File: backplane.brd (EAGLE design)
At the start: 153.7 x 128.3 mm, 55 parts, among them J1 L717HDE15PD4CH4R, J10 5013310807, J11 5013310807, J12 5013310807, J13 5013310807, J14 5013311007, J15 5013311007, J16 5013311007, J17 5013311007, J18 5013311007, J19 5013311007, J2 1054301102, J20 5013311007, J21 5013311007, J22 5013311007, J23 5013311007, J24 SEAM-40-03.0-S-06-2-A-K-TR, J25 5055670271, J3 5011902017, J4 5013310807, J5 5013310807, J6 5013310807, J7 5013310807, J8 5013310807, J9 5013310807, U1 AM26LV32EIPWR, U10 AM26LV32EIPWR, U2 AM26LV32EIPWR, U3 AM26LV32EIPWR, U4 AM26LV32EIPWR, U5 AM26LV32EIPWR, U6 AM26LV32EIPWR, U7 AM26LV32EIPWR, U8 AM26LV32EIPWR, U9 AM26LV32EIPWR

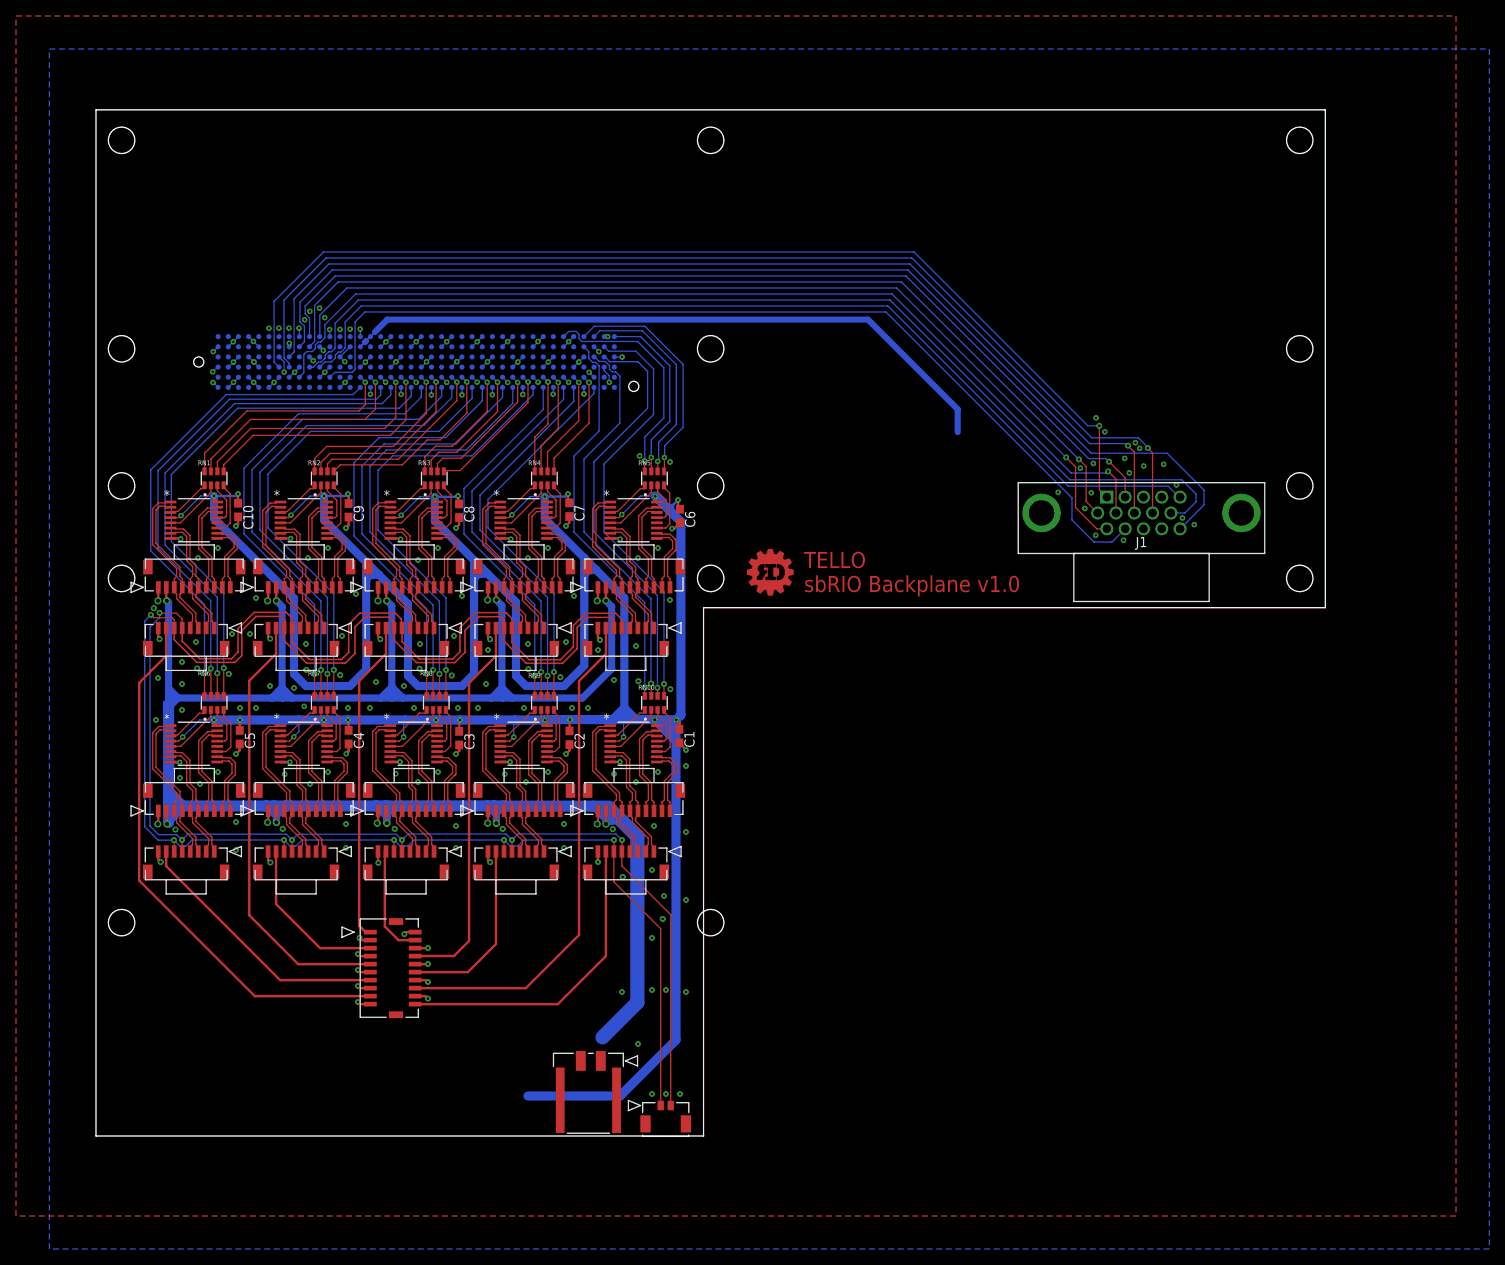
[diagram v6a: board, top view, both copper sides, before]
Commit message: added filter, 3v3 reg, and extra DIO
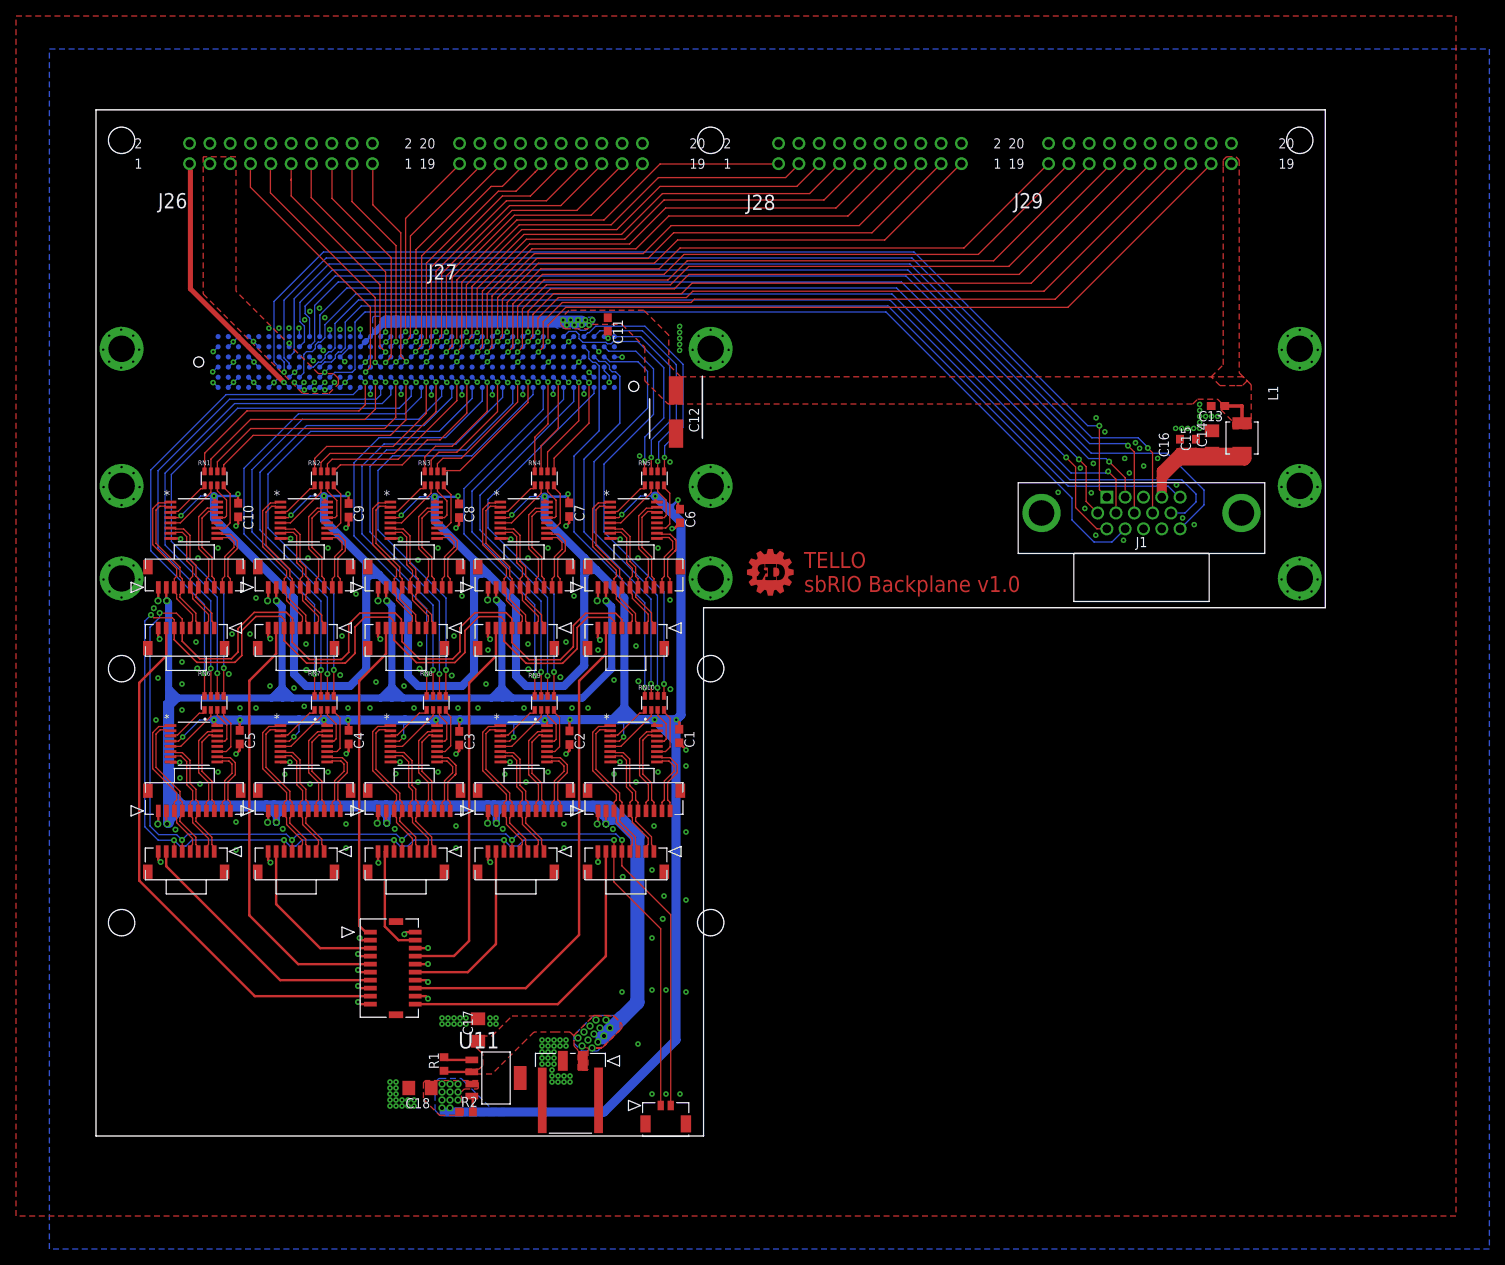
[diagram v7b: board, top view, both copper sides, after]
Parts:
- added C11: 4.7uF, rcl:C0603
- added C12: 875105144010, sbrio_backplane:CAPAE660X580N
- added C13: (no value), rcl:C0603
- added C14: 100uF, rcl:C1206
- added C15: 0.1uF, rcl:C0603
- added C16: 0.01uF, rcl:C0603
- added C17: 68uF, rcl:C1206
- added C18: 33uF, rcl:C1206
- added J26, J27, J28, J29: SAMTEC-TST-110-01-X-DJ, sbrio_backplane:SAMTEC-TST-110-01-X-D
- added L1: 74437324068, sbrio_backplane:WE-LHMI_402048
- added R1, R2: 10K, rcl:R0603
- added U11: LP3962EMP-3.3, sbrio_backplane:SOT150P696X180-5N
- moved J2 2.25 mm to (60.9, 9.39)
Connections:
- new net 3V3_SBRIO: J24.F8, J26.1
- new net 5V_SBRIO: J24.F10, J24.F11, J24.F12, J24.F9, J26.3, J26.5
- new net DIO18: J24.C36
- new net DIO19: J24.C35
- new net DIO20: J24.C33
- new net DIO21: J24.C32, J29.15
- new net DIO22: J24.C30, J29.7
- new net DIO23: J24.C29, J29.3
- new net DIO24: J24.C27, J28.15
- new net DIO25: J24.C26, J28.11
- new net DIO26: J24.C24, J28.3
- new net DIO27: J24.C23, J27.19
- new net DIO28: J24.C21, J27.11
- new net DIO29: J24.C20, J27.7
- new net DIO30: J24.C18, J26.15
- new net DIO31: J24.C17, J26.11
- new net DIO50: J24.B36
- new net DIO51: J24.B34
- new net DIO52: J24.B33, J29.17
- new net DIO53: J24.B31, J29.11
- new net DIO54: J24.B30, J29.5
- new net DIO55: J24.B28, J28.19
- new net DIO56: J24.B27, J28.13
- new net DIO57: J24.B25, J28.7
- new net DIO58: J24.B24, J28.1
- new net DIO59: J24.B22, J27.15
- new net DIO60: J24.B21, J27.9
- new net DIO61: J24.B19, J27.3
- new net DIO62: J24.B18, J26.17
- new net DIO85: J24.A32, J29.13
- new net DIO86: J24.A31, J29.9
- new net DIO87: J24.A29, J29.1
- new net DIO88: J24.A28, J28.17
- new net DIO89: J24.A26, J28.9
- new net DIO90: J24.A25, J28.5
- new net DIO91: J24.A23, J27.17
- new net DIO92: J24.A22, J27.13
- new net DIO93: J24.A20, J27.5
- new net DIO94: J24.A19, J27.1
- new net DIO95: J24.A17, J26.13
- new net N$1: R1.2, U11.1
- new net N$15: J24.B16
- new net N$2: R2.2, U11.4
- net 3V3: now also C18.1, R2.1, U11.3
- net 5V: now also C17.1, J2.1, R1.1, U11.2
- net 5V_C_SERIES: now also C11.1, C12.1, C13.1, J29.19, L1.1
- net 5V_FILT: now also C14.1, C15.1, C16.1, L1.2
- net DIO77: now also J26.19
- net DIO78: now also J26.9
- net DIO79: now also J26.7
- net GND: now also C11.2, C12.2, C13.2, C14.2, C15.2, C16.2, C17.2, C18.2, J2.2, J2.3, J2.4, J26.10, J26.12, J26.14, J26.16, J26.18, J26.2, J26.20, J26.4, J26.6, J26.8, J27.10, J27.12, J27.14, J27.16, J27.18, J27.2, J27.20, J27.4, J27.6, J27.8, J28.10, J28.12, J28.14, J28.16, J28.18, J28.2, J28.20, J28.4, J28.6, J28.8, J29.10, J29.12, J29.14, J29.16, J29.18, J29.2, J29.20, J29.4, J29.6, J29.8, U11.5
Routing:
- net DIO52: track 0.00 -> 94.2 mm, vias 0 -> 1
- net DIO21: track 0.00 -> 94.1 mm, vias 0 -> 1
- net DIO85: track 0.00 -> 89.7 mm, vias 0 -> 1
- net DIO53: track 0.00 -> 89.6 mm, vias 0 -> 1
- net DIO22: track 0.00 -> 87.6 mm, vias 0 -> 1
- net DIO86: track 0.00 -> 86.3 mm, vias 0 -> 1
- net DIO54: track 0.00 -> 84.2 mm, vias 0 -> 1
- net DIO23: track 0.00 -> 84.0 mm, vias 0 -> 1
- net DIO87: track 0.00 -> 79.4 mm, vias 0 -> 1
- net DIO55: track 0.00 -> 70.9 mm, vias 0 -> 1
- net DIO24: track 0.00 -> 68.6 mm, vias 0 -> 1
- net DIO88: track 0.00 -> 67.6 mm, vias 0 -> 1
- net DIO56: track 0.00 -> 65.3 mm, vias 0 -> 1
- net DIO25: track 0.00 -> 65.1 mm, vias 0 -> 1
- net DIO89: track 0.00 -> 60.7 mm, vias 0 -> 1
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- added copper zone on layer 1, net 3V3
- added copper zone on layer 16, net 3V3
- added copper zone on layer 1, net 5V
- added copper zone on layer 16, net 5V
- added copper zone on layer 1, net 5V_C_SERIES
- added copper zone on layer 16, net 5V_C_SERIES
- added copper zone on layer 1, net 5V_SBRIO
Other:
- board text removed: "DO MOUNTING HOLES NEED TO BE GROUNDED"
